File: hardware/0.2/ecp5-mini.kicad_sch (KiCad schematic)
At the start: 22 parts, among them J3 S7 Mini, J4 S7 Mini, U1 ECP5U_12_CABGA256, X1 DSC6101CI2A-016.0000

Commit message: routing++
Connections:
- net LED_4: now also U1.M6 (PL47A/+/HS/LDQ44)
- net LED_5: now also U1.M5 (PL44C/+/LDQ44)
- net LED_6: now also U1.R5 (PL44A/+/HS/LDQS44)
- net LED_7: now also U1.T4 (PL44B/-/HS/LDQSN44)
- net PG04+: now also U1.L1 (PL26A/+/PCLKT6_1/HS/LDQ32)
- net PG04-: now also U1.L2 (PL26B/-/PCLKC6_1/HS/LDQ32)
- net PG15+: now also U1.K4 (PL29A/+/GR_PCLK6_0/HS/LDQ32)
- net PG15-: now also U1.K5 (PL29B/-/HS/LDQ32)
- net PH04+: now also U1.R4 (PL41C/+/LDQ44)
- net PH04-: now also U1.T3 (PL41D/-/LDQ44)
- net PH15+: now also U1.P4 (PL41A/+/HS/LDQ44)
- net PH15-: now also U1.R3 (PL41B/-/HS/LDQ44)
- net PH26+: now also U1.R2 (PL38C/+/LDQ44)
- net PH26-: now also U1.T2 (PL38D/-/LDQ44)
- net PH37+: now also U1.P1 (PL35A/+/HS/LDQ32)
- net PH37-: now also U1.R1 (PL35B/-/VREF1_6/HS/LDQ32)
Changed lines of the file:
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@@
     (company "Josh Johnson")
   )
+  (bus_alias "SD" (members "SD_DAT[0..3]" "SD_CMD" "SD_CLK" "SD_DET"))
+  (bus_alias "HYPERRAM" (members "HR_nRST" "HR_nCS" "HR_CK_N" "HR_RWDS" "HR_DQ[0..7]" "HR_CK" "HR_nCK"))
+  (bus_alias "USB" (members "USB_D-" "USB_D+" "USB_PU"))
   (bus_alias "LED" (members "LED_[0..7]" "LED_R" "LED_G" "LED_B"))
-  (bus_alias "USB" (members "USB_D-" "USB_D+" "USB_PU"))
-  (bus_alias "HYPERRAM" (members "HR_nRST" "HR_nCS" "HR_CK_N" "HR_RWDS" "HR_DQ[0..7]" "HR_CK" "HR_nCK"))
-  (bus_alias "SD" (members "SD_DAT[0..3]" "SD_CMD" "SD_CLK" "SD_DET"))
   (junction (at 60.96 62.23) (diameter 1.016) (color 0 0 0 0))
   (junction (at 62.23 176.53) (diameter 1.016) (color 0 0 0 0))
@@
   (junction (at 358.14 196.85) (diameter 1.016) (color 0 0 0 0))
   (junction (at 358.14 198.12) (diameter 1.016) (color 0 0 0 0))
-  (no_connect (at 215.9 200.66))
-  (no_connect (at 215.9 261.62))
-  (no_connect (at 215.9 218.44))
+  (no_connect (at 215.9 246.38))
+  (no_connect (at 215.9 215.9))
+  (no_connect (at 215.9 220.98))
   (no_connect (at 215.9 236.22))
-  (no_connect (at 215.9 205.74))
+  (no_connect (at 215.9 203.2))
+  (no_connect (at 215.9 208.28))
   (no_connect (at 215.9 223.52))
-  (no_connect (at 215.9 215.9))
   (no_connect (at 215.9 269.24))
   (no_connect (at 215.9 238.76))
-  (no_connect (at 215.9 220.98))
-  (no_connect (at 215.9 208.28))
+  (no_connect (at 215.9 218.44))
+  (no_connect (at 215.9 200.66))
+  (no_connect (at 215.9 205.74))
+  (no_connect (at 215.9 271.78))
+  (no_connect (at 215.9 261.62))
   (no_connect (at 215.9 266.7))
-  (no_connect (at 215.9 246.38))
-  (no_connect (at 215.9 271.78))
-  (no_connect (at 215.9 203.2))
   (bus_entry (at 62.23 81.28) (size 2.54 2.54)
     (stroke (width 0.1524) (type solid) (color 0 0 0 0))
@@
     (stroke (width 0.1524) (type solid) (color 0 0 0 0))
   )
-  (bus_entry (at 160.02 110.49) (size 2.54 -2.54)
-    (stroke (width 0.1524) (type solid) (color 0 0 0 0))
-  )
-  (bus_entry (at 160.02 113.03) (size 2.54 -2.54)
-    (stroke (width 0.1524) (type solid) (color 0 0 0 0))
-  )
-  (bus_entry (at 160.02 115.57) (size 2.54 -2.54)
-    (stroke (width 0.1524) (type solid) (color 0 0 0 0))
-  )
-  (bus_entry (at 160.02 118.11) (size 2.54 -2.54)
+  (bus_entry (at 148.59 142.24) (size 2.54 -2.54)
+    (stroke (width 0.1524) (type solid) (color 0 0 0 0))
+  )
+  (bus_entry (at 148.59 144.78) (size 2.54 -2.54)
+    (stroke (width 0.1524) (type solid) (color 0 0 0 0))
+  )
+  (bus_entry (at 148.59 147.32) (size 2.54 -2.54)
+    (stroke (width 0.1524) (type solid) (color 0 0 0 0))
+  )
+  (bus_entry (at 148.59 152.4) (size 2.54 -2.54)
     (stroke (width 0.1524) (type solid) (color 0 0 0 0))
   )
@@
     (stroke (width 0) (type solid) (color 0 0 0 0))
   )
+  (wire (pts (xy 137.16 81.28) (xy 148.59 81.28))
+    (stroke (width 0) (type solid) (color 0 0 0 0))
+  )
+  (wire (pts (xy 137.16 83.82) (xy 148.59 83.82))
+    (stroke (width 0) (type solid) (color 0 0 0 0))
+  )
+  (wire (pts (xy 137.16 91.44) (xy 148.59 91.44))
+    (stroke (width 0) (type solid) (color 0 0 0 0))
+  )
+  (wire (pts (xy 137.16 93.98) (xy 148.59 93.98))
+    (stroke (width 0) (type solid) (color 0 0 0 0))
+  )
+  (wire (pts (xy 137.16 111.76) (xy 148.59 111.76))
+    (stroke (width 0) (type solid) (color 0 0 0 0))
+  )
+  (wire (pts (xy 137.16 114.3) (xy 148.59 114.3))
+    (stroke (width 0) (type solid) (color 0 0 0 0))
+  )
+  (wire (pts (xy 137.16 127) (xy 148.59 127))
+    (stroke (width 0) (type solid) (color 0 0 0 0))
+  )
+  (wire (pts (xy 137.16 129.54) (xy 148.59 129.54))
+    (stroke (width 0) (type solid) (color 0 0 0 0))
+  )
+  (wire (pts (xy 137.16 132.08) (xy 148.59 132.08))
+    (stroke (width 0) (type solid) (color 0 0 0 0))
+  )
+  (wire (pts (xy 137.16 134.62) (xy 148.59 134.62))
+    (stroke (width 0) (type solid) (color 0 0 0 0))
+  )
+  (wire (pts (xy 137.16 137.16) (xy 148.59 137.16))
+    (stroke (width 0) (type solid) (color 0 0 0 0))
+  )
+  (wire (pts (xy 137.16 139.7) (xy 148.59 139.7))
+    (stroke (width 0) (type solid) (color 0 0 0 0))
+  )
+  (wire (pts (xy 137.16 142.24) (xy 148.59 142.24))
+    (stroke (width 0) (type solid) (color 0 0 0 0))
+  )
+  (wire (pts (xy 137.16 144.78) (xy 148.59 144.78))
+    (stroke (width 0) (type solid) (color 0 0 0 0))
+  )
+  (wire (pts (xy 137.16 147.32) (xy 148.59 147.32))
+    (stroke (width 0) (type solid) (color 0 0 0 0))
+  )
+  (wire (pts (xy 137.16 152.4) (xy 148.59 152.4))
+    (stroke (width 0) (type solid) (color 0 0 0 0))
+  )
   (wire (pts (xy 138.43 190.5) (xy 144.78 190.5))
     (stroke (width 0) (type solid) (color 0 0 0 0))
@@
     (stroke (width 0) (type solid) (color 0 0 0 0))
   )
-  (wire (pts (xy 148.59 110.49) (xy 160.02 110.49))
-    (stroke (width 0) (type solid) (color 0 0 0 0))
-  )
-  (wire (pts (xy 148.59 113.03) (xy 160.02 113.03))
-    (stroke (width 0) (type solid) (color 0 0 0 0))
-  )
-  (wire (pts (xy 148.59 115.57) (xy 160.02 115.57))
-    (stroke (width 0) (type solid) (color 0 0 0 0))
-  )
-  (wire (pts (xy 148.59 118.11) (xy 160.02 118.11))
-    (stroke (width 0) (type solid) (color 0 0 0 0))
-  )
   (wire (pts (xy 156.21 175.26) (xy 156.21 176.53))
     (stroke (width 0) (type solid) (color 0 0 0 0))
@@
     (stroke (width 0) (type solid) (color 0 0 0 0))
   )
-  (wire (pts (xy 160.02 100.33) (xy 148.59 100.33))
-    (stroke (width 0) (type solid) (color 0 0 0 0))
-  )
-  (wire (pts (xy 160.02 102.87) (xy 148.59 102.87))
+  (wire (pts (xy 157.48 86.36) (xy 168.91 86.36))
+    (stroke (width 0) (type solid) (color 0 0 0 0))
+  )
+  (wire (pts (xy 157.48 88.9) (xy 168.91 88.9))
+    (stroke (width 0) (type solid) (color 0 0 0 0))
+  )
+  (wire (pts (xy 157.48 91.44) (xy 168.91 91.44))
+    (stroke (width 0) (type solid) (color 0 0 0 0))
+  )
+  (wire (pts (xy 157.48 93.98) (xy 168.91 93.98))
+    (stroke (width 0) (type solid) (color 0 0 0 0))
+  )
+  (wire (pts (xy 162.56 100.33) (xy 151.13 100.33))
+    (stroke (width 0) (type solid) (color 0 0 0 0))
+  )
+  (wire (pts (xy 162.56 102.87) (xy 151.13 102.87))
     (stroke (width 0) (type solid) (color 0 0 0 0))
   )
@@
     (effects (font (size 1.27 1.27)) (justify right bottom))
   )
-  (label "LED_4" (at 158.75 110.49 180)
-    (effects (font (size 1.27 1.27)) (justify right bottom))
-  )
-  (label "LED_5" (at 158.75 113.03 180)
-    (effects (font (size 1.27 1.27)) (justify right bottom))
-  )
-  (label "LED_6" (at 158.75 115.57 180)
-    (effects (font (size 1.27 1.27)) (justify right bottom))
-  )
-  (label "LED_7" (at 158.75 118.11 180)
-    (effects (font (size 1.27 1.27)) (justify right bottom))
-  )
-  (label "LED_USR" (at 160.02 100.33 180)
-    (effects (font (size 1.27 1.27)) (justify right bottom))
-  )
-  (label "LED_ACT" (at 160.02 102.87 180)
-    (effects (font (size 1.27 1.27)) (justify right bottom))
-  )
+  (label "LED_6" (at 147.32 142.24 180)
+    (effects (font (size 1.27 1.27)) (justify right bottom))
+  )
+  (label "LED_7" (at 147.32 144.78 180)
+    (effects (font (size 1.27 1.27)) (justify right bottom))
+  )
+  (label "LED_5" (at 147.32 147.32 180)
+    (effects (font (size 1.27 1.27)) (justify right bottom))
+  )
+  (label "LED_4" (at 147.32 152.4 180)
+    (effects (font (size 1.27 1.27)) (justify right bottom))
+  )
+  (label "PG04+" (at 148.59 81.28 180)
+    (effects (font (size 1.27 1.27)) (justify right bottom))
+  )
+  (label "PG04-" (at 148.59 83.82 180)
+    (effects (font (size 1.27 1.27)) (justify right bottom))
+  )
+  (label "PG15+" (at 148.59 91.44 180)
+    (effects (font (size 1.27 1.27)) (justify right bottom))
+  )
+  (label "PG15-" (at 148.59 93.98 180)
+    (effects (font (size 1.27 1.27)) (justify right bottom))
+  )
+  (label "PH37+" (at 148.59 111.76 180)
+    (effects (font (size 1.27 1.27)) (justify right bottom))
+  )
+  (label "PH37-" (at 148.59 114.3 180)
+    (effects (font (size 1.27 1.27)) (justify right bottom))
+  )
+  (label "PH26+" (at 148.59 127 180)
+    (effects (font (size 1.27 1.27)) (justify right bottom))
+  )
+  (label "PH26-" (at 148.59 129.54 180)
+    (effects (font (size 1.27 1.27)) (justify right bottom))
+  )
+  (label "PH15+" (at 148.59 132.08 180)
+    (effects (font (size 1.27 1.27)) (justify right bottom))
+  )
+  (label "PH15-" (at 148.59 134.62 180)
+    (effects (font (size 1.27 1.27)) (justify right bottom))
+  )
+  (label "PH04+" (at 148.59 137.16 180)
+    (effects (font (size 1.27 1.27)) (justify right bottom))
+  )
+  (label "PH04-" (at 148.59 139.7 180)
+    (effects (font (size 1.27 1.27)) (justify right bottom))
+  )
+  (label "LED_USR" (at 162.56 100.33 180)
+    (effects (font (size 1.27 1.27)) (justify right bottom))
+  )
+  (label "LED_ACT" (at 162.56 102.87 180)
+    (effects (font (size 1.27 1.27)) (justify right bottom))
+  )
+  (label "PG26+" (at 168.91 86.36 180)
+    (effects (font (size 1.27 1.27)) (justify right bottom))
+  )
+  (label "PG26-" (at 168.91 88.9 180)
+    (effects (font (size 1.27 1.27)) (justify right bottom))
+  )
+  (label "PG37+" (at 168.91 91.44 180)
+    (effects (font (size 1.27 1.27)) (justify right bottom))
+  )
+  (label "PG37-" (at 168.91 93.98 180)
+    (effects (font (size 1.27 1.27)) (justify right bottom))
+  )

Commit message: unrouted = 0
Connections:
- net LED_ACT: now also U1.B2 (PL2B/-/HS/LDQ8)
- net LED_USR: now also U1.B1 (PL2A/+/HS/LDQ8)
- net PE04+: now also U1.F2 (PL11C/+/LDQ8)
- net PE04-: now also U1.E1 (PL11D/-/LDQ8)
- net PE15+: now also U1.C1 (PL5A/+/HS/LDQ8)
- net PE15-: now also U1.C2 (PL5B/-/HS/LDQ8)
- net PE26+: now also U1.C3 (PL2C/+/LDQ8)
- net PE26-: now also U1.D3 (PL2D/-/LDQ8)
- net PE37+: now also U1.E3 (PL5C/+/LDQ8)
- net PE37-: now also U1.F3 (PL5D/-/LDQ8)
- net PF04+: now also U1.J1 (PL23A/+/PCLKT7_1/HS/LDQ20)
- net PF04-: now also U1.J2 (PL23B/-/PCLKC7_1/HS/LDQ20)
- net PF15+: now also U1.G1 (PL20A/+/GR_PCLK7_1/HS/LDQS20)
- net PF15-: now also U1.H2 (PL20B/-/HS/LDQSN20)
- net PF26+: now also U1.F1 (PL14A/+/HS/LDQ20)
- net PF26-: now also U1.G2 (PL14B/-/HS/LDQ20)
- net PF37+: now also U1.G5 (PL11A/+/HS/LDQ8)
- net PF37-: now also U1.G4 (PL11B/-/HS/LDQ8)
- net PG04+: now also U1.N1 (PL32A/+/HS/LDQS32); no longer U1.L1 (PL26A/+/PCLKT6_1/HS/LDQ32)
- net PG04-: now also U1.P2 (PL32B/-/HS/LDQSN32); no longer U1.L2 (PL26B/-/PCLKC6_1/HS/LDQ32)
- net PG26+: now also U1.L1 (PL26A/+/PCLKT6_1/HS/LDQ32)
- net PG26-: now also U1.L2 (PL26B/-/PCLKC6_1/HS/LDQ32)
- net PG37+: now also U1.H5 (PL17A/+/HS/LDQ20)
- net PG37-: now also U1.H4 (PL17B/-/HS/LDQ20)
- no-connect marks 15 -> 83

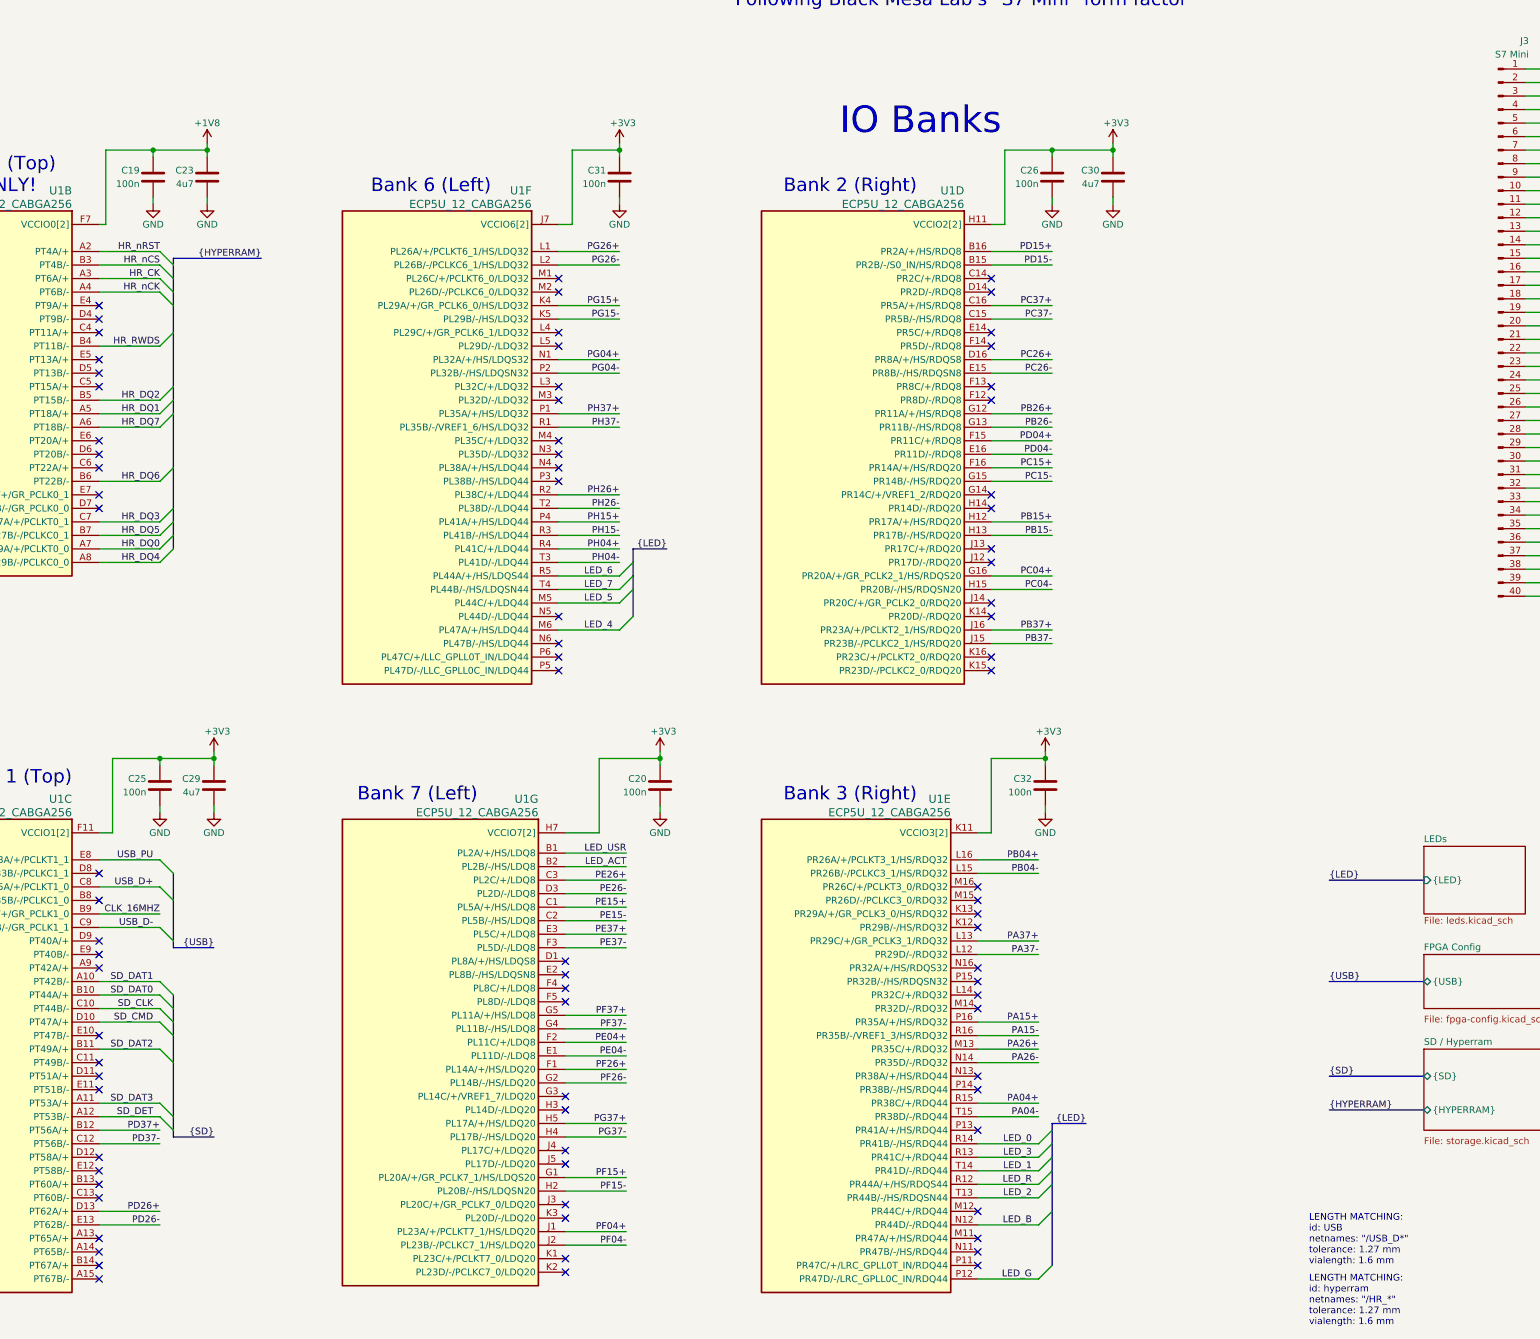
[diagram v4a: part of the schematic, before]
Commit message: hyperram now length matched
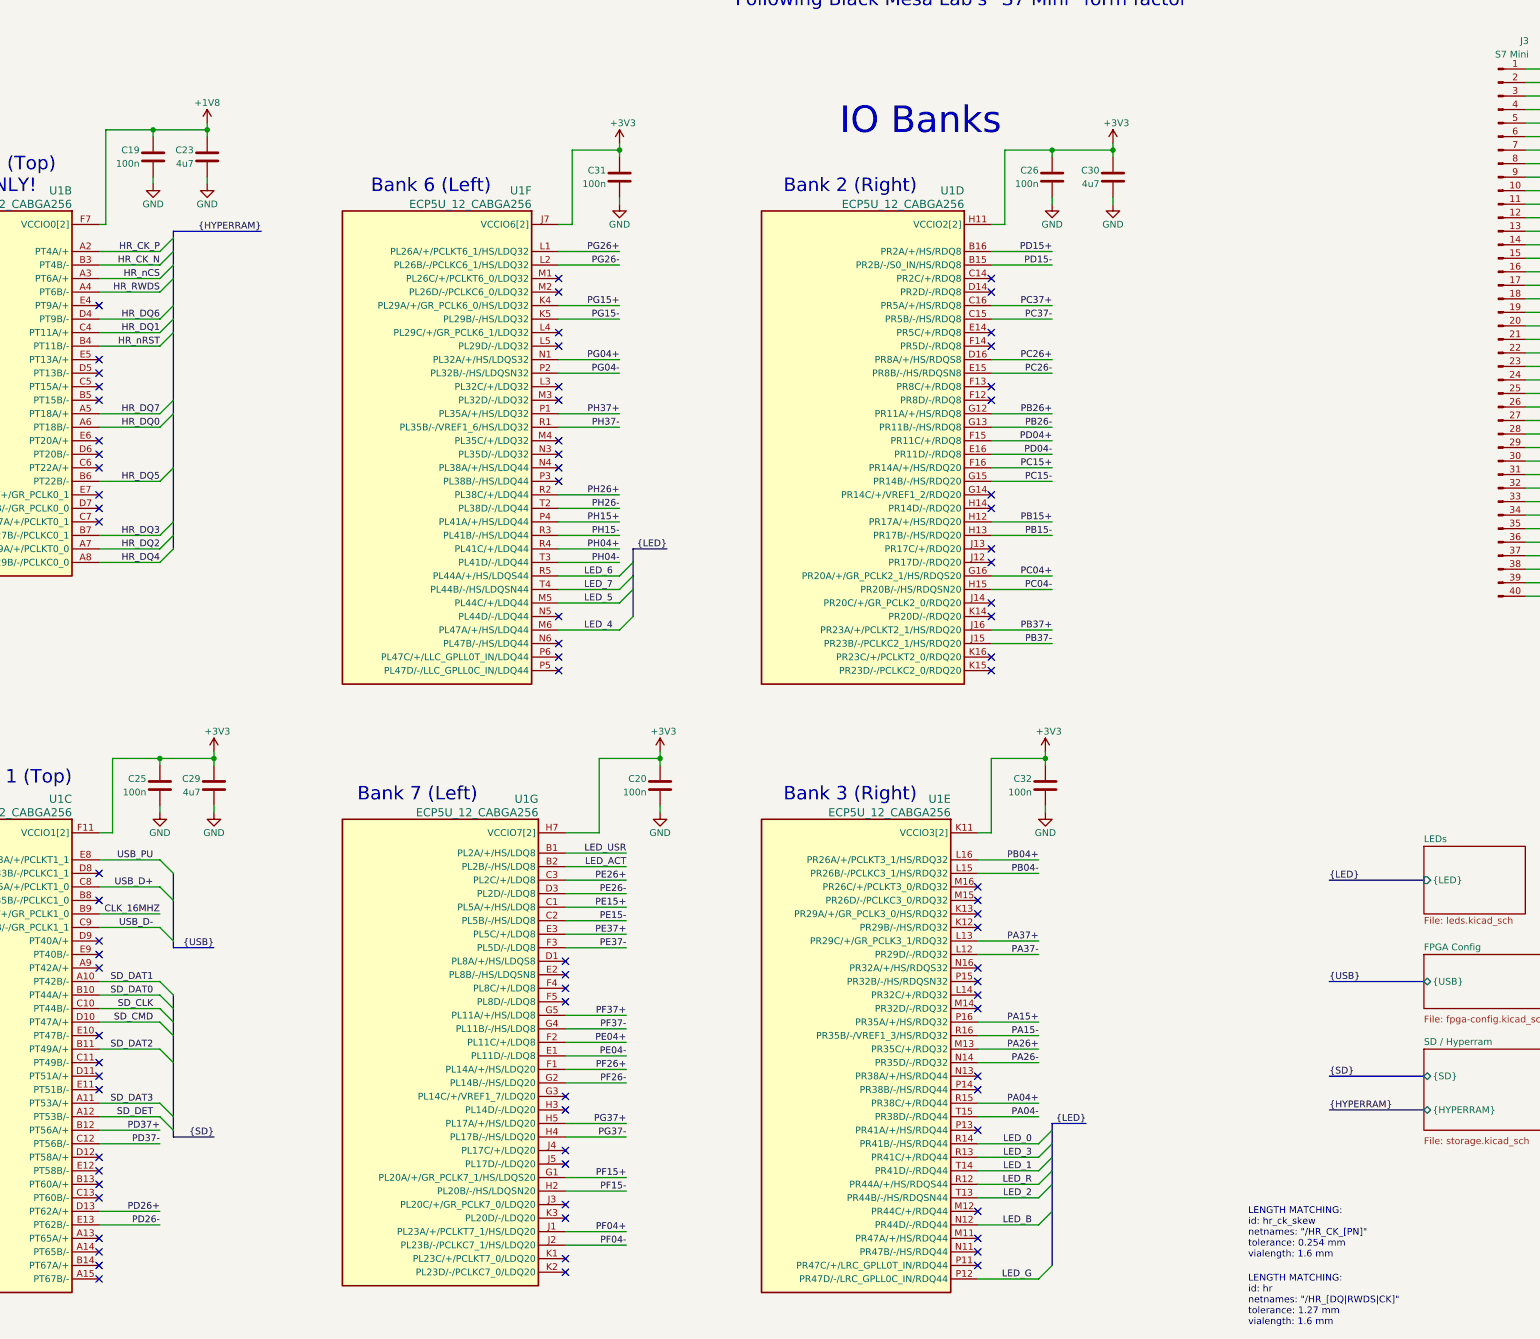
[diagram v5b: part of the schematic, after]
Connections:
- net HR_CK is gone; now on net HR_nCS: U1.A3 (PT6A/+)
- net HR_nCK is gone; now on net HR_RWDS: U1.A4 (PT6B/-)
- net HR_DQ0: now also U1.A6 (PT18B/-); no longer U1.A7 (PT29A/+/PCLKT0_0)
- net HR_DQ1: now also U1.C4 (PT11A/+); no longer U1.A5 (PT18A/+)
- net HR_DQ2: now also U1.A7 (PT29A/+/PCLKT0_0); no longer U1.B5 (PT15B/-)
- net HR_DQ3: now also U1.B7 (PT27B/-/PCLKC0_1); no longer U1.C7 (PT27A/+/PCLKT0_1)
- net HR_DQ5: now also U1.B6 (PT22B/-); no longer U1.B7 (PT27B/-/PCLKC0_1)
- net HR_DQ6: now also U1.D4 (PT9B/-); no longer U1.B6 (PT22B/-)
- net HR_DQ7: now also U1.A5 (PT18A/+); no longer U1.A6 (PT18B/-)
- net HR_RWDS: no longer U1.B4 (PT11B/-)
- net HR_nCS: no longer U1.B3 (PT4B/-)
- net HR_nRST: now also U1.B4 (PT11B/-); no longer U1.A2 (PT4A/+)
- new net HR_CK_N: U1.B3 (PT4B/-)
- new net HR_CK_P: U1.A2 (PT4A/+)
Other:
- note added: "LENGTH MATCHING: id: hr netnames: "/HR_[DQ|RWDS|CK]" tolerance: 1.27 mm vialength: 1.6 mm"
- note added: "LENGTH MATCHING: id: hr_ck_skew netnames: "/HR_CK_[PN]" tolerance: 0.254 mm vialength: 1.6 mm"
- note removed: "LENGTH MATCHING: id: USB netnames: "/USB_D*" tolerance: 1.27 mm vialength: 1.6 mm"
- note removed: "LENGTH MATCHING: id: hyperram netnames: "/HR_*" tolerance: 1.27 mm vialength: 1.6 mm"
- moved on the sheet: C19, C23
